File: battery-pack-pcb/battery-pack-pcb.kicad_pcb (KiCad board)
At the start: 2 copper layers, 55 x 34 mm, 7 parts, among them J1 Conn_01x02_Female, J2 Conn_01x02_Female

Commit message: Add capacitor to battery pack
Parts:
- added C1: C_Small, Capacitor_SMD:C_1210_3225Metric_Pad1.42x2.65mm_HandSolder, F.Cu at (77.5, 77.0)
- moved D1 2.00 mm to (83.5, 77.0)
- moved D2 2.00 mm to (71.5, 77.0)
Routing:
- net Net-(C1-Pad1): track 28.9 -> 42.3 mm
- net Net-(BT1-Pad2): track 112.7 -> 114.1 mm
- net Net-(BT1-Pad1): track 40.7 -> 39.5 mm
- net Net-(BT2-Pad1): track 40.7 -> 39.5 mm
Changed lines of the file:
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@@
     (thickness 1.6)
     (drawings 16)
-    (tracks 33)
+    (tracks 40)
     (zones 0)
-    (modules 7)
+    (modules 8)
     (nets 5)
   )
@@
   (net 2 "Net-(BT1-Pad1)")
   (net 3 "Net-(BT2-Pad1)")
-  (net 4 "Net-(D1-Pad1)")
+  (net 4 "Net-(C1-Pad1)")
   (net_class Default "これはデフォルトのネット クラスです。"
     (clearance 0.2)
@@
     (add_net "Net-(BT1-Pad2)")
     (add_net "Net-(BT2-Pad1)")
-    (add_net "Net-(D1-Pad1)")
+    (add_net "Net-(C1-Pad1)")
+  )
+  (module Capacitor_SMD:C_1210_3225Metric_Pad1.42x2.65mm_HandSolder (layer F.Cu)
+    (at 77.5 77 90)
+    (descr "Capacitor SMD 1210 (3225 Metric), square (rectangular) end terminal, IPC_7351 nominal with elongated pad for handsoldering. (Body size source: http://www.tortai-tech.com/upload/download/2011102023233369053.pdf), generated with kicad-footprint-generator")
+    (tags "capacitor handsolder")
+    (attr smd)
+    (fp_text reference C1 (at 0 -2.28 90) (layer F.SilkS)
+      (effects (font (size 1 1) (thickness 0.15)))
+    )
+    (fp_text value C_Small (at 0 2.28 90) (layer F.Fab)
+      (effects (font (size 1 1) (thickness 0.15)))
+    )
+    (fp_text user %R (at 0 0 90) (layer F.Fab)
+      (effects (font (size 0.8 0.8) (thickness 0.12)))
+    )
+    (fp_line (start 2.45 1.58) (end -2.45 1.58) (layer F.CrtYd) (width 0.05))
+    (fp_line (start 2.45 -1.58) (end 2.45 1.58) (layer F.CrtYd) (width 0.05))
+    (fp_line (start -2.45 -1.58) (end 2.45 -1.58) (layer F.CrtYd) (width 0.05))
+    (fp_line (start -2.45 1.58) (end -2.45 -1.58) (layer F.CrtYd) (width 0.05))
+    (fp_line (start -0.602064 1.36) (end 0.602064 1.36) (layer F.SilkS) (width 0.12))
+    (fp_line (start -0.602064 -1.36) (end 0.602064 -1.36) (layer F.SilkS) (width 0.12))
+    (fp_line (start 1.6 1.25) (end -1.6 1.25) (layer F.Fab) (width 0.1))
+    (fp_line (start 1.6 -1.25) (end 1.6 1.25) (layer F.Fab) (width 0.1))
+    (fp_line (start -1.6 -1.25) (end 1.6 -1.25) (layer F.Fab) (width 0.1))
+    (fp_line (start -1.6 1.25) (end -1.6 -1.25) (layer F.Fab) (width 0.1))
+    (pad 2 smd roundrect (at 1.4875 0 90) (size 1.425 2.65) (layers F.Cu F.Paste F.Mask) (roundrect_rratio 0.175439)
+      (net 1 "Net-(BT1-Pad2)"))
+    (pad 1 smd roundrect (at -1.4875 0 90) (size 1.425 2.65) (layers F.Cu F.Paste F.Mask) (roundrect_rratio 0.175439)
+      (net 4 "Net-(C1-Pad1)"))
+    (model ${KISYS3DMOD}/Capacitor_SMD.3dshapes/C_1210_3225Metric.wrl
+      (at (xyz 0 0 0))
+      (scale (xyz 1 1 1))
+      (rotate (xyz 0 0 0))
+    )
   )
   (module MountingHole:MountingHole_2.2mm_M2 (layer F.Cu)
@@
       (net 1 "Net-(BT1-Pad2)"))
     (pad 2 thru_hole oval (at 2 0 90) (size 1.2 1.75) (drill 0.75) (layers *.Cu *.Mask)
-      (net 4 "Net-(D1-Pad1)"))
+      (net 4 "Net-(C1-Pad1)"))
     (model ${KISYS3DMOD}/Connector_JST.3dshapes/JST_PH_S2B-PH-K_1x02_P2.00mm_Horizontal.wrl
       (at (xyz 0 0 0))
@@
       (net 1 "Net-(BT1-Pad2)"))
     (pad 2 thru_hole oval (at 2 0 270) (size 1.2 1.75) (drill 0.75) (layers *.Cu *.Mask)
-      (net 4 "Net-(D1-Pad1)"))
+      (net 4 "Net-(C1-Pad1)"))
     (model ${KISYS3DMOD}/Connector_JST.3dshapes/JST_PH_S2B-PH-K_1x02_P2.00mm_Horizontal.wrl
       (at (xyz 0 0 0))
@@
   )
   (module Diode_SMD:D_SOD-123 (layer F.Cu)
-    (at 73.5 77 90)
+    (at 71.5 77 90)
     (descr SOD-123)
     (tags SOD-123)
@@
     (fp_line (start -2.25 -1) (end 1.65 -1) (layer F.SilkS) (width 0.12))
     (pad 1 smd rect (at -1.65 0 90) (size 0.9 1.2) (layers F.Cu F.Paste F.Mask)
-      (net 4 "Net-(D1-Pad1)"))
+      (net 4 "Net-(C1-Pad1)"))
     (pad 2 smd rect (at 1.65 0 90) (size 0.9 1.2) (layers F.Cu F.Paste F.Mask)
       (net 3 "Net-(BT2-Pad1)"))
@@
   )
   (module Diode_SMD:D_SOD-123 (layer F.Cu)
-    (at 81.5 77 90)
+    (at 83.5 77 90)
     (descr SOD-123)
     (tags SOD-123)
@@
     (fp_line (start -2.25 -1) (end 1.65 -1) (layer F.SilkS) (width 0.12))
     (pad 1 smd rect (at -1.65 0 90) (size 0.9 1.2) (layers F.Cu F.Paste F.Mask)
-      (net 4 "Net-(D1-Pad1)"))
+      (net 4 "Net-(C1-Pad1)"))
     (pad 2 smd rect (at 1.65 0 90) (size 0.9 1.2) (layers F.Cu F.Paste F.Mask)
       (net 2 "Net-(BT1-Pad1)"))
@@
   (segment (start 92 63.5) (end 102 63.5) (width 0.25) (layer F.Cu) (net 1))
   (segment (start 102 63.5) (end 103 64.5) (width 0.25) (layer F.Cu) (net 1))
+  (segment (start 64 79.5) (end 66.5 77) (width 0.25) (layer F.Cu) (net 1))
+  (segment (start 76.0125 77) (end 77.5 75.5125) (width 0.25) (layer F.Cu) (net 1))
+  (segment (start 73.75 77) (end 76.0125 77) (width 0.25) (layer F.Cu) (net 1))
+  (segment (start 66.5 77) (end 73.75 77) (width 0.25) (layer F.Cu) (net 1))
   (segment (start 91.67071 80.82929) (end 91 81.5) (width 0.25) (layer F.Cu) (net 1))
   (segment (start 93 79.5) (end 91.67071 80.82929) (width 0.25) (layer F.Cu) (net 1))
-  (segment (start 93 78.5) (end 93 79.5) (width 0.25) (layer F.Cu) (net 1))
-  (segment (start 91.5 77) (end 93 78.5) (width 0.25) (layer F.Cu) (net 1))
-  (segment (start 64 79.5) (end 66.5 77) (width 0.25) (layer F.Cu) (net 1))
-  (segment (start 66.5 77) (end 91.5 77) (width 0.25) (layer F.Cu) (net 1))
-  (segment (start 81.5 73.6) (end 81.5 75.35) (width 0.25) (layer F.Cu) (net 2))
+  (segment (start 93 78.25) (end 93 79.5) (width 0.25) (layer F.Cu) (net 1))
+  (segment (start 91.75 77) (end 93 78.25) (width 0.25) (layer F.Cu) (net 1))
+  (segment (start 77.5 75.5125) (end 78.9875 77) (width 0.25) (layer F.Cu) (net 1))
+  (segment (start 78.9875 77) (end 91.75 77) (width 0.25) (layer F.Cu) (net 1))
+  (segment (start 95.70635 75.35) (end 99.778175 71.278175) (width 0.25) (layer F.Cu) (net 2))
+  (segment (start 83.6 75.35) (end 95.70635 75.35) (width 0.25) (layer F.Cu) (net 2))
+  (segment (start 81.5 73.25) (end 83.6 75.35) (width 0.25) (layer F.Cu) (net 2))
   (segment (start 84.221825 55.721825) (end 81.5 58.44365) (width 0.25) (layer F.Cu) (net 2))
-  (segment (start 81.5 58.44365) (end 81.5 73.6) (width 0.25) (layer F.Cu) (net 2))
-  (segment (start 95.70635 75.35) (end 99.778175 71.278175) (width 0.25) (layer F.Cu) (net 2))
-  (segment (start 81.5 75.35) (end 95.70635 75.35) (width 0.25) (layer F.Cu) (net 2))
-  (segment (start 73.5 58.44365) (end 73.5 75.35) (width 0.25) (layer F.Cu) (net 3))
+  (segment (start 81.5 58.44365) (end 81.5 73.25) (width 0.25) (layer F.Cu) (net 2))
+  (segment (start 59.29365 75.35) (end 55.221825 71.278175) (width 0.25) (layer F.Cu) (net 3))
+  (segment (start 71.5 75.35) (end 59.29365 75.35) (width 0.25) (layer F.Cu) (net 3))
+  (segment (start 73.5 73.35) (end 71.5 75.35) (width 0.25) (layer F.Cu) (net 3))
   (segment (start 70.778175 55.721825) (end 73.5 58.44365) (width 0.25) (layer F.Cu) (net 3))
-  (segment (start 59.29365 75.35) (end 55.221825 71.278175) (width 0.25) (layer F.Cu) (net 3))
-  (segment (start 73.5 75.35) (end 59.29365 75.35) (width 0.25) (layer F.Cu) (net 3))
+  (segment (start 73.5 58.44365) (end 73.5 73.35) (width 0.25) (layer F.Cu) (net 3))
+  (segment (start 83.5 78.65) (end 71.5 78.65) (width 0.25) (layer F.Cu) (net 4))
+  (segment (start 89.875 79.5) (end 87.875 81.5) (width 0.25) (layer F.Cu) (net 4))
+  (segment (start 91 79.5) (end 89.875 79.5) (width 0.25) (layer F.Cu) (net 4))
+  (segment (start 80.5125 81.5) (end 77.5 78.4875) (width 0.25) (layer F.Cu) (net 4))
+  (segment (start 87.875 81.5) (end 80.5125 81.5) (width 0.25) (layer F.Cu) (net 4))
   (segment (start 65.125 81.5) (end 64 81.5) (width 0.25) (layer F.Cu) (net 4))
-  (segment (start 71.35 81.5) (end 65.125 81.5) (width 0.25) (layer F.Cu) (net 4))
-  (segment (start 73.5 79.35) (end 71.35 81.5) (width 0.25) (layer F.Cu) (net 4))
-  (segment (start 73.5 78.65) (end 73.5 79.35) (width 0.25) (layer F.Cu) (net 4))
-  (segment (start 81.5 78.65) (end 73.5 78.65) (width 0.25) (layer F.Cu) (net 4))
-  (segment (start 90.15 78.65) (end 91 79.5) (width 0.25) (layer F.Cu) (net 4))
-  (segment (start 81.5 78.65) (end 90.15 78.65) (width 0.25) (layer F.Cu) (net 4))
+  (segment (start 74.525 81.5) (end 65.125 81.5) (width 0.25) (layer F.Cu) (net 4))
+  (segment (start 77.5 78.4875) (end 77.5 78.525) (width 0.25) (layer F.Cu) (net 4))
+  (segment (start 77.5 78.525) (end 74.525 81.5) (width 0.25) (layer F.Cu) (net 4))
 )

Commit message: Update silk of battery pack pcb
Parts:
- J1, J2: footprint Connector_JST:JST_PH_S2B-PH-K_1x02_P2.00mm_Horizontal -> locallib:JST_PH_S2B-PH-K_1x02_P2.00mm_Horizontal_nosilk
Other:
- board text added: "Battery Pack v1.1"
- board text added: "GND"
- board text added: "VCC"

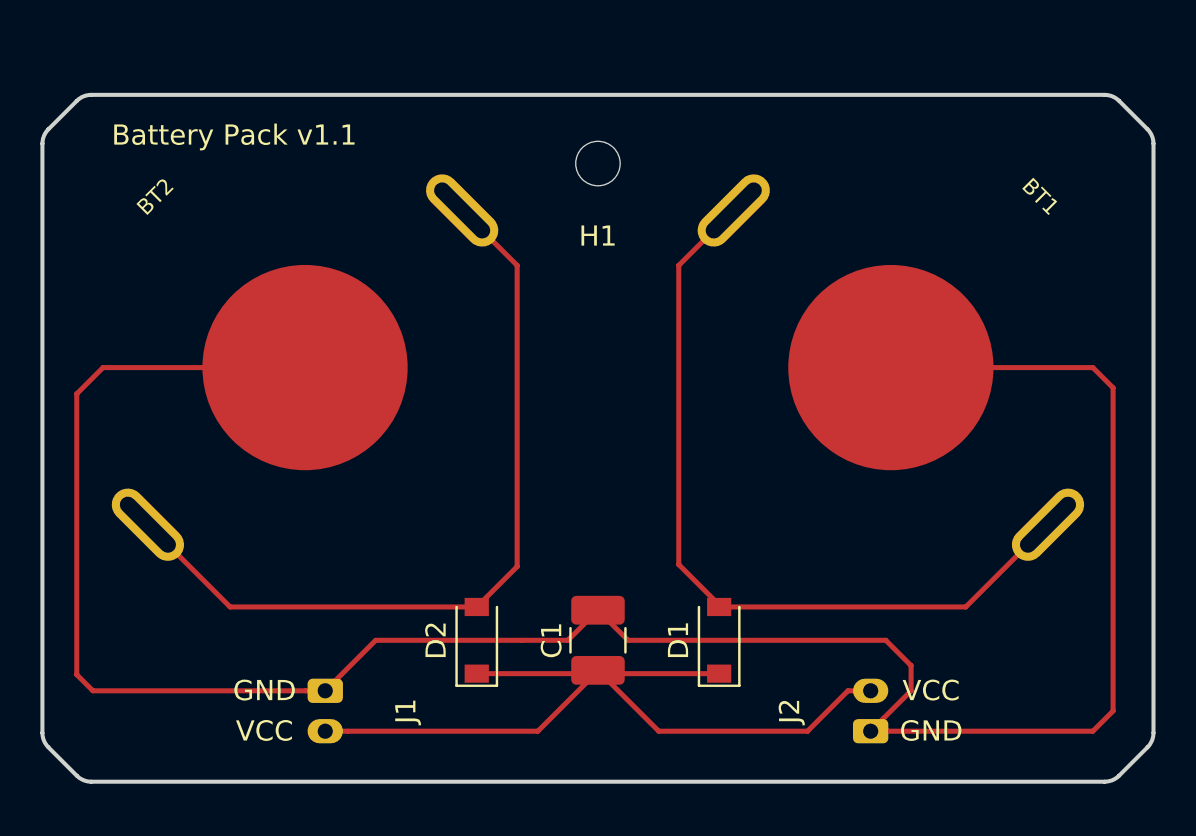
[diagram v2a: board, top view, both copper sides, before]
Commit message: Add power switch to battery PCB
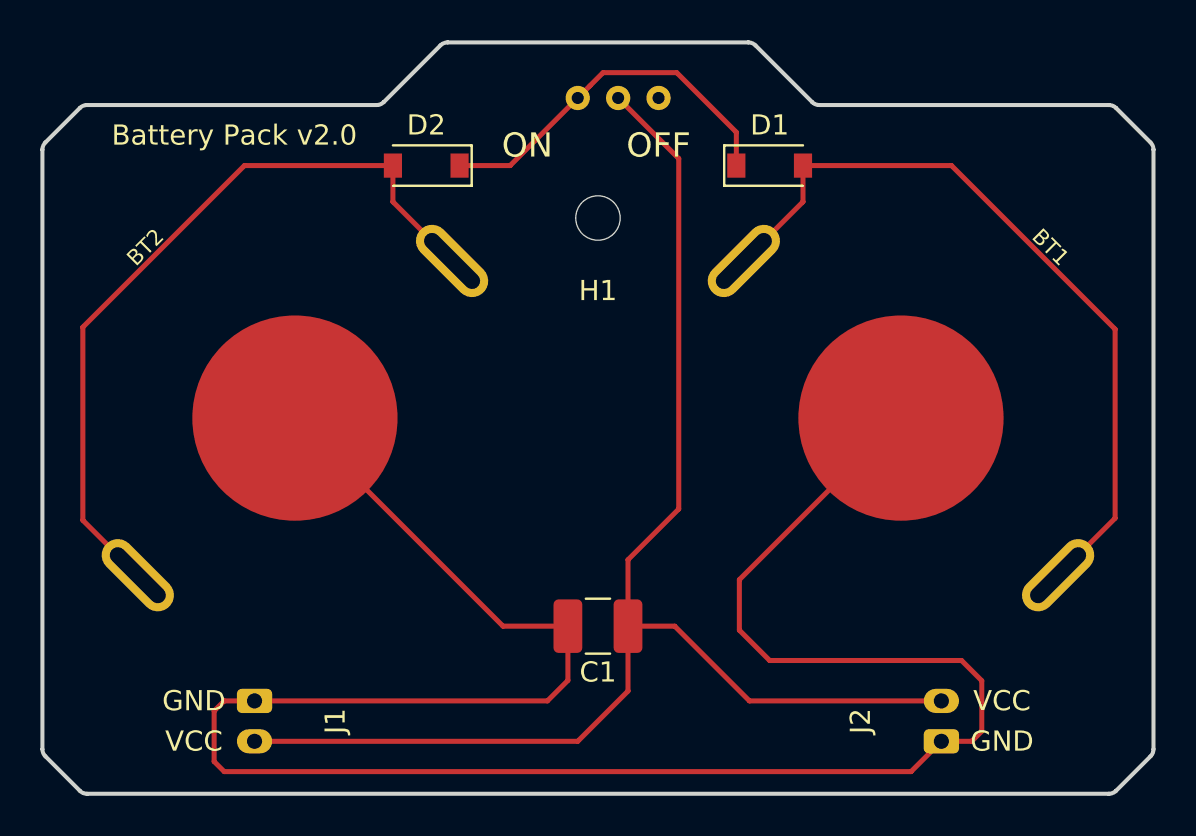
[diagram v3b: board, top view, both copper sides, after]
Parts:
- added SW1: SW_Push_SPDT, locallib:slide_switch_vertical_01x03_pitch2mm, B.Cu at (80.5, 50.2)
- moved D1 23.6 mm to (86.0, 53.5), turned to 0 degrees
- moved D2 23.6 mm to (69.0, 53.5), turned to 180 degrees
- moved J1 3.54 mm to (60.5, 80.0)
- moved J2 3.54 mm to (94.5, 82.0)
- moved H1 2.70 mm to (77.5, 56.1)
- moved BT1 2.55 mm to (92.5, 66.0)
- moved BT2 2.55 mm to (62.5, 66.0)
- moved C1 0.70 mm to (77.5, 76.3), turned to 180 degrees
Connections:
- D1 pad 1: Net-(C1-Pad1) -> Net-(D1-Pad1)
- D2 pad 1: Net-(C1-Pad1) -> Net-(D1-Pad1)
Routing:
- net Net-(C1-Pad1): track 42.3 -> 68.2 mm
- net Net-(D1-Pad1): track 0.00 -> 18.5 mm
- net Net-(BT1-Pad2): track 114.1 -> 109.5 mm
- net Net-(BT2-Pad1): track 39.5 -> 38.0 mm
- net Net-(BT1-Pad1): track 39.5 -> 38.1 mm
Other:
- board size 55 x 34 mm -> 55 x 37.2 mm
- board text added: "Battery Pack v2.0"
- board text added: "OFF"
- board text added: "ON"
- board text removed: "Battery Pack v1.1"

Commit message: Adjust silk & hole size of battery pack
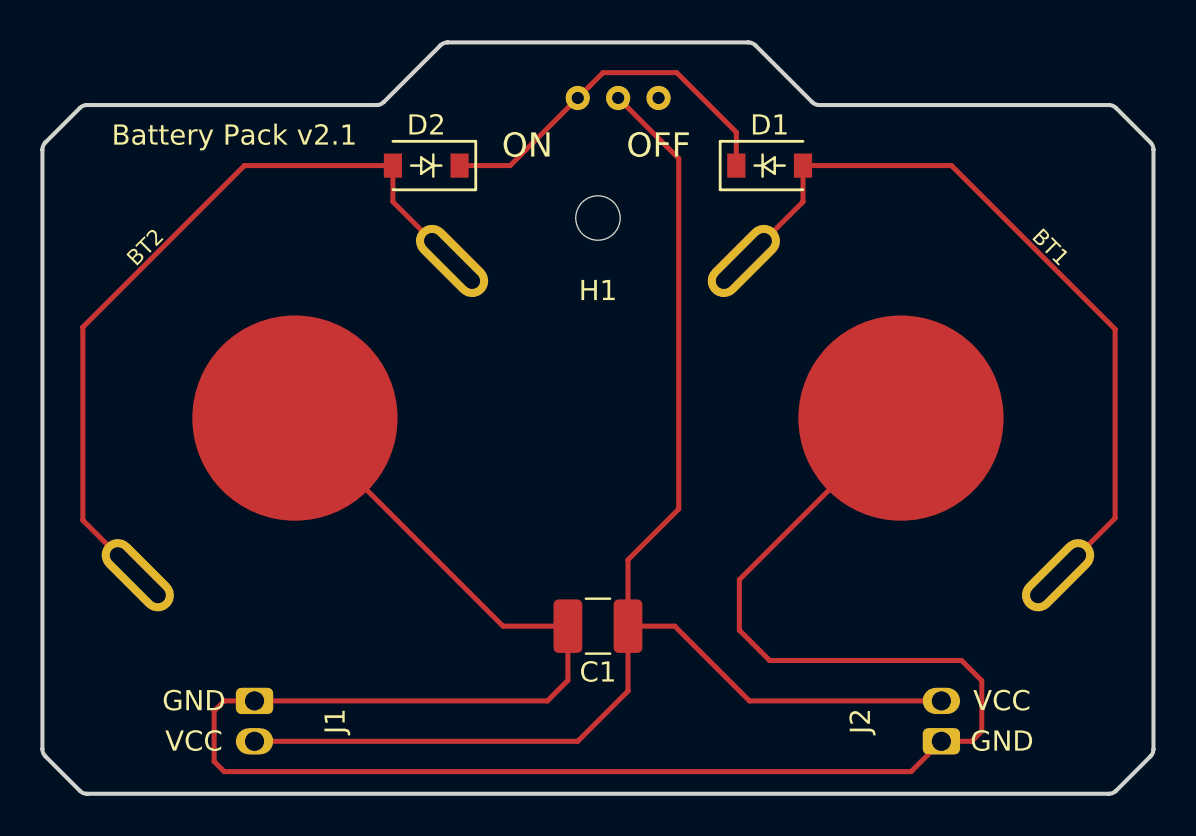
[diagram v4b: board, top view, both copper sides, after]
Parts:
- D1, D2: footprint Diode_SMD:D_SOD-123 -> locallib:D_SOD-123
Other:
- board text added: "Battery Pack v2.1"
- board text removed: "Battery Pack v2.0"
